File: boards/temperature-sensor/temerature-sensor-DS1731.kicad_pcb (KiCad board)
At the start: 2 copper layers, 19.1 x 26.7 mm, 10 parts, among them J1 CONN_01X04_MALE, U1 DS1731U

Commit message: requested changes added
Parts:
- renumbered REF** to M3
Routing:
- net Net-(R5-Pad2): track 12.3 -> 16.0 mm, vias 0 -> 2
- net Net-(R3-Pad2): track 13.2 -> 16.5 mm, vias 0 -> 2
- net /VDD: track 35.0 -> 37.5 mm, vias 5 -> 2
- net /GND: track 32.5 -> 31.9 mm
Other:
- net class Default: trace_width 0.25 -> 0.6
- board text added: "GND"
- board text added: "SCL"
- board text added: "SDA"
- board text added: "VDD"
- board text added: "rexus-viper DS1731 temp sense board"

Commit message: added labels, keepout areas
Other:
- board text added: "© Richard Chojetzki"
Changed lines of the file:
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@@
     (area 123.114999 100.254999 142.315001 127.075001)
     (thickness 1.6)
-    (drawings 9)
+    (drawings 10)
     (tracks 67)
     (zones 0)
@@
     (pad 1 np_thru_hole circle (at 0 0) (size 3.2 3.2) (drill 3.2) (layers *.Cu *.Mask))
   )
+  (gr_text "© Richard\nChojetzki" (at 130.81 107.95 90) (layer B.SilkS)
+    (effects (font (size 1.5 1.5) (thickness 0.3)) (justify mirror))
+  )
   (gr_text "rexus-viper\nDS1731 temp\nsense board" (at 137.16 118.11 90) (layer B.SilkS)
     (effects (font (size 1.5 1.5) (thickness 0.3)) (justify mirror))
@@
   (segment (start 131.445 112.395) (end 130.81 111.76) (width 0.6) (layer F.Cu) (net 4))
   (segment (start 139.7 121.92) (end 140.97 120.65) (width 0.6) (layer F.Cu) (net 5))
-  (segment (start 140.335 112.395) (end 138.59 112.395) (width 0.6) (layer F.Cu) (net 5) (status 800000))
+  (segment (start 140.335 112.395) (end 138.59 112.395) (width 0.6) (layer F.Cu) (net 5))
   (segment (start 140.97 113.03) (end 140.335 112.395) (width 0.6) (layer F.Cu) (net 5))
   (segment (start 140.97 120.65) (end 140.97 113.03) (width 0.6) (layer F.Cu) (net 5))
@@
   (segment (start 137.16 121.92) (end 138.43 120.65) (width 0.6) (layer B.Cu) (net 6))
   (via (at 137.16 121.92) (size 0.6) (drill 0.4) (layers F.Cu B.Cu) (net 6))
-  (segment (start 136.525 113.665) (end 138.59 113.665) (width 0.6) (layer F.Cu) (net 6) (status 800000))
+  (segment (start 136.525 113.665) (end 138.59 113.665) (width 0.6) (layer F.Cu) (net 6))
   (segment (start 135.89 114.3) (end 136.525 113.665) (width 0.6) (layer F.Cu) (net 6))
   (via (at 135.89 114.3) (size 0.6) (drill 0.4) (layers F.Cu B.Cu) (net 6))

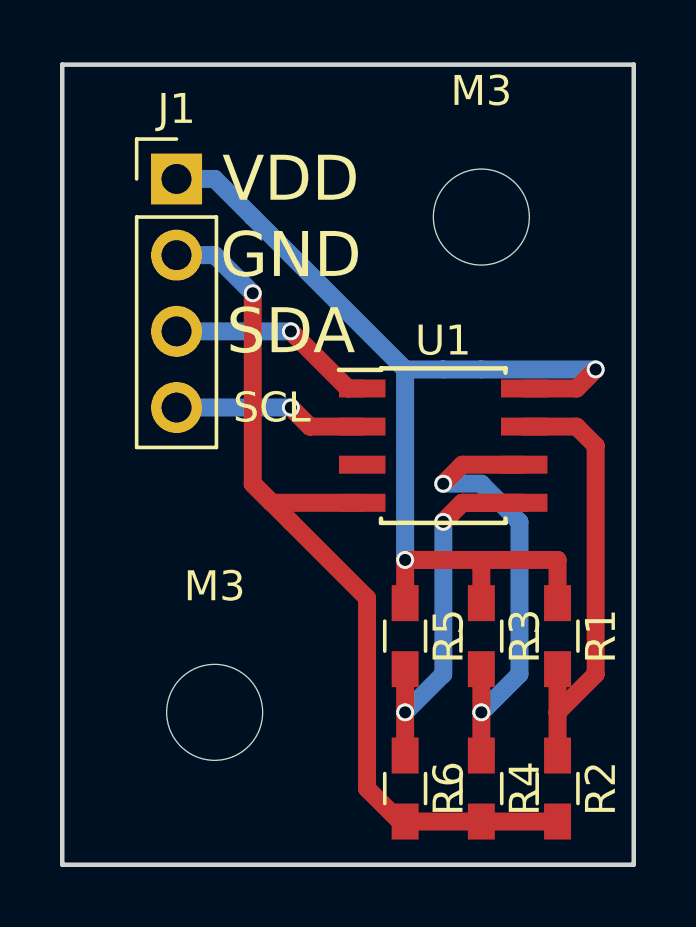
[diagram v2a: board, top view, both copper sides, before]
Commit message: added solder-jumpers
the clearance at the jumpers looks prettey small,
is this allright?
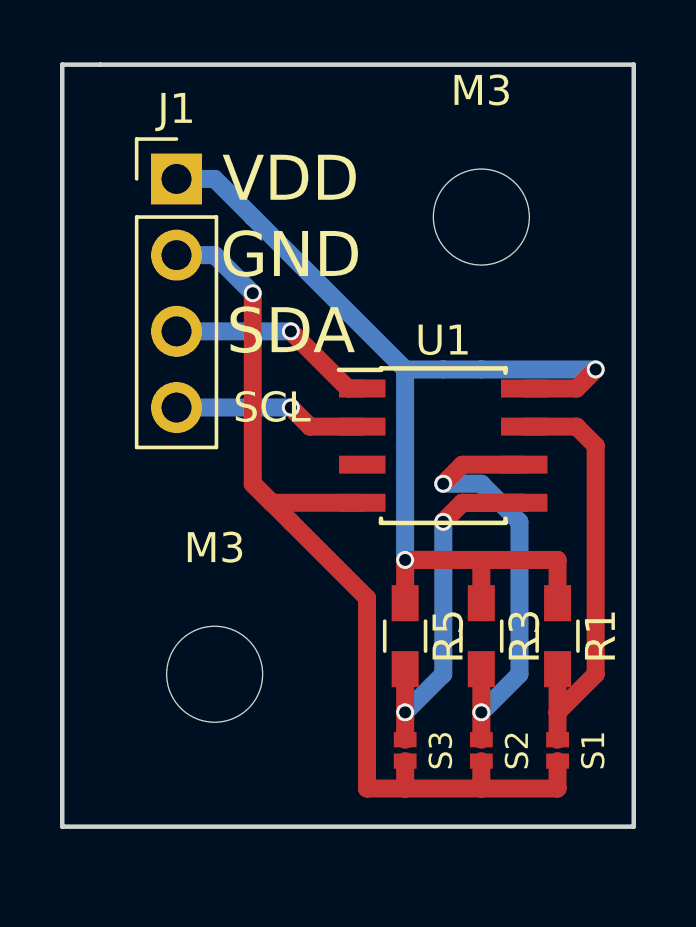
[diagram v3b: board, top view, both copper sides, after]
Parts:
- removed R2, R4, R6: R, Resistors_SMD:R_0603_HandSoldering
- added S1: S_JUMPER, rchojetzki-temp-board-footprint-lib:S_JUMPER_2_rchojetzki, F.Cu at (139.7, 123.2)
- added S2: S_JUMPER, rchojetzki-temp-board-footprint-lib:S_JUMPER_2_rchojetzki, F.Cu at (137.2, 123.2)
- added S3: S_JUMPER, rchojetzki-temp-board-footprint-lib:S_JUMPER_2_rchojetzki, F.Cu at (134.6, 123.2)
- moved M3 1.27 mm to (128.3, 120.7)
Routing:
- net /GND: track 31.9 -> 34.2 mm
- net Net-(R5-Pad2): track 16.0 -> 15.2 mm
- net Net-(R3-Pad2): track 16.5 -> 15.7 mm
- net Net-(R1-Pad2): track 14.9 -> 14.4 mm
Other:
- board size 19.1 x 26.7 mm -> 19.1 x 25.4 mm
- net class Default: clearance 0.2 -> 0.1
- rule trace_clearance: 0.2 -> 0.1
